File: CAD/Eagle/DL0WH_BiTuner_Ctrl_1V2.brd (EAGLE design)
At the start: 96.5 x 73 mm, 141 parts, among them Q0321 ABS07-32.768KHZ, U0101 STM32L476RXT_64PIN_LDO, U0601 MC33996, U0701 MC33996, U0801 MC33996, U0921 TS5A23166, U0951 OPA354, U1001 MAX232_SOIC16, U1101 MAX232_SOIC16, U1201 LM53603-Q1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

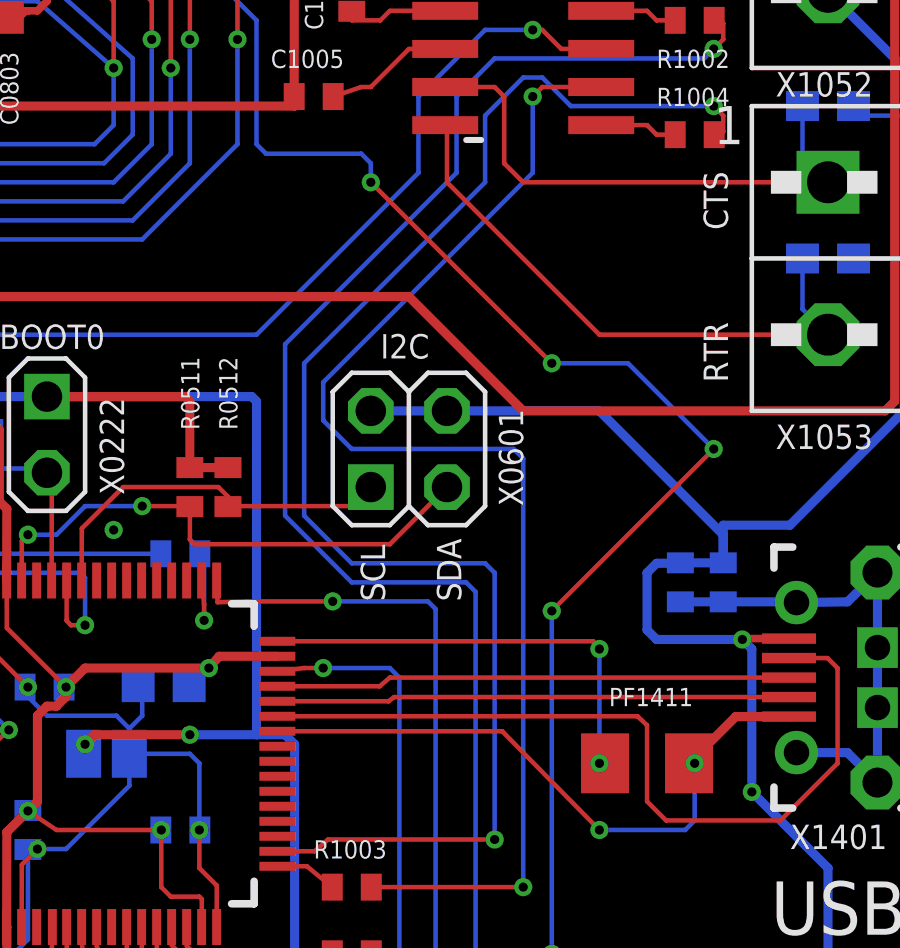
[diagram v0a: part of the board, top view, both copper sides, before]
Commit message: HW_1V2 - CAD/Eagle - add CRS08 to power the 5V rail when no 12V is attached
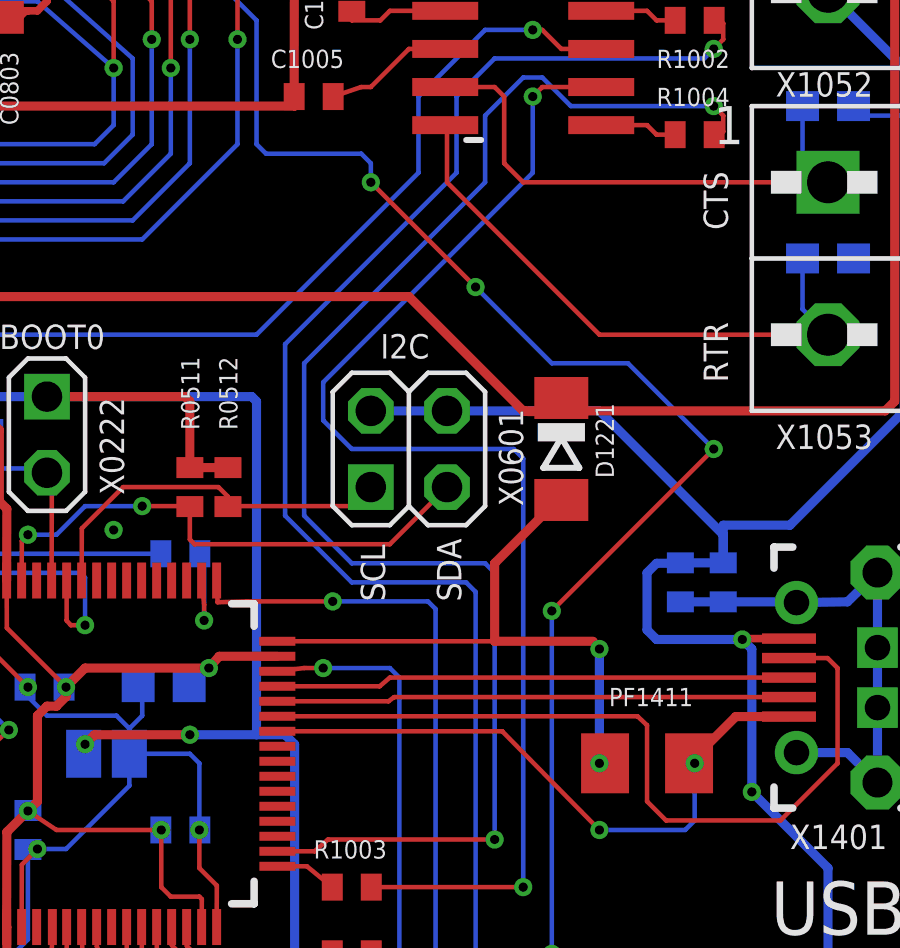
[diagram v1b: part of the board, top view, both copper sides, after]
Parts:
- added D1221: CRS08, df4iah_diode:SOD80C
- C0311: value 18pF -> 22pF
- C0332: value 8.2pF -> 18pF
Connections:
- net +5V: now also D1221.C
- net VDDUSB: now also D1221.A
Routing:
- net VDDUSB: track 15.1 -> 20.8 mm
- net +5V: track 286.2 -> 287.6 mm
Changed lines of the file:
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@@
 <attribute name="VALUE" x="61.08" y="24.5575" size="0.6096" layer="27" font="vector" ratio="10" rot="R180"/>
 </element>
-<element name="C0311" library="df4iah_rcl" package="C0402" value="18pF" x="57.62625" y="18.7325" smashed="yes" rot="R270">
+<element name="C0311" library="df4iah_rcl" package="C0402" value="22pF" x="57.62625" y="18.7325" smashed="yes" rot="R270">
 <attribute name="NAME" x="56.515" y="17.30375" size="0.6096" layer="25" font="vector" ratio="10" rot="R90"/>
 <attribute name="VALUE" x="55.72125" y="19.3675" size="0.6096" layer="27" font="vector" ratio="10" rot="R270"/>
@@
 <attribute name="VALUE" x="74.93" y="7.14375" size="0.6096" layer="28" font="vector" ratio="10" rot="MR180"/>
 </element>
-<element name="C0332" library="df4iah_rcl" package="C0402" value="8.2pF" x="60.96" y="24.4475" smashed="yes" rot="R90">
+<element name="C0332" library="df4iah_rcl" package="C0402" value="18pF" x="60.96" y="24.4475" smashed="yes" rot="R90">
 <attribute name="NAME" x="60.16625" y="23.1775" size="0.6096" layer="25" font="vector" ratio="10" rot="R90"/>
 <attribute name="VALUE" x="62.865" y="23.8125" size="0.6096" layer="27" font="vector" ratio="10" rot="R90"/>
@@
 <attribute name="VALUE" x="76.2" y="1.27" size="0.8128" layer="27" font="vector" ratio="15"/>
 </element>
+<element name="D1221" library="df4iah_diode" package="SOD80C" value="CRS08" x="83.82" y="29.21" rot="R270"/>
 </elements>
 <signals>
@@
 <via x="10.16" y="33.02" extent="1-16" drill="0.3048"/>
 <via x="17.62125" y="26.51125" extent="1-16" drill="0.3048"/>
+<wire x1="65.745" y1="56.72" x2="68.58" y2="58.42" width="0" layer="19" extent="1-1"/>
+<wire x1="15.3875" y1="53.295" x2="14.2875" y2="53.295" width="0" layer="19" extent="1-1"/>
+<wire x1="13.1875" y1="53.295" x2="14.2875" y2="53.295" width="0" layer="19" extent="1-1"/>
+<wire x1="15.3875" y1="54.595" x2="15.3875" y2="53.295" width="0" layer="19" extent="1-1"/>
+<wire x1="14.2875" y1="54.595" x2="15.3875" y2="54.595" width="0" layer="19" extent="1-1"/>
+<wire x1="14.2875" y1="55.245" x2="14.2875" y2="54.595" width="0" layer="19" extent="1-1"/>
+<wire x1="14.2875" y1="55.245" x2="14.2875" y2="55.245" width="0" layer="19" extent="1-16"/>
+<wire x1="14.2875" y1="55.895" x2="14.2875" y2="55.245" width="0" layer="19" extent="1-1"/>
+<wire x1="15.3875" y1="55.895" x2="14.2875" y2="55.895" width="0" layer="19" extent="1-1"/>
+<wire x1="13.1875" y1="55.895" x2="14.2875" y2="55.895" width="0" layer="19" extent="1-1"/>
+<wire x1="13.1875" y1="54.595" x2="14.2875" y2="54.595" width="0" layer="19" extent="1-1"/>
+<wire x1="15.3875" y1="57.195" x2="15.3875" y2="55.895" width="0" layer="19" extent="1-1"/>
+<wire x1="14.2875" y1="57.195" x2="15.3875" y2="57.195" width="0" layer="19" extent="1-1"/>
+<wire x1="13.1875" y1="57.195" x2="14.2875" y2="57.195" width="0" layer="19" extent="1-1"/>
+<wire x1="55.88" y1="20.32" x2="57.62625" y2="18.0825" width="0" layer="19" extent="1-1"/>
+<wire x1="17.62125" y1="26.51125" x2="14.605" y2="28.2575" width="0" layer="19" extent="1-1"/>
+<wire x1="68.8975" y1="26.51125" x2="65.3375" y2="27.21375" width="0" layer="19" extent="1-1"/>
+<wire x1="10.16" y1="33.02" x2="13.97" y2="31.75" width="0" layer="19" extent="16-16"/>
 </signal>
 <signal name="VDDUSB">
 <contactref element="PF1411" pad="2"/>
 <contactref element="U0101" pad="48"/>
-<wire x1="74.355" y1="22.8" x2="84.8825" y2="22.8" width="0.1524" layer="1"/>
+<wire x1="74.355" y1="22.8" x2="81.5975" y2="22.8" width="0.1524" layer="1"/>
+<wire x1="81.5975" y1="22.8" x2="84.8825" y2="22.8" width="0.3048" layer="1"/>
 <wire x1="84.8825" y1="22.8" x2="85.09" y2="22.5425" width="0.1524" layer="1"/>
 <via x="85.09" y="22.5425" extent="1-16" drill="0.3048"/>
-<wire x1="85.09" y1="22.5425" x2="85.09" y2="18.7325" width="0.1524" layer="16"/>
+<wire x1="85.09" y1="22.5425" x2="85.09" y2="18.7325" width="0.3048" layer="16"/>
 <via x="85.09" y="18.7325" extent="1-16" drill="0.3048"/>
 <wire x1="85.09" y1="18.7325" x2="85.09" y2="18.92" width="0.1524" layer="1"/>
 <wire x1="85.09" y1="18.92" x2="85.2775" y2="18.7325" width="0.1524" layer="1"/>
+<contactref element="D1221" pad="A"/>
+<wire x1="83.82" y1="27.51" x2="83.7075" y2="27.51" width="0.3048" layer="1"/>
+<wire x1="83.7075" y1="27.51" x2="81.5975" y2="25.4" width="0.3048" layer="1"/>
+<wire x1="81.5975" y1="25.4" x2="81.5975" y2="22.8" width="0.3048" layer="1"/>
 </signal>
 <signal name="MCU_VREF_M">
@@
 <wire x1="86.0575" y1="51.1175" x2="86.375" y2="51.435" width="0.3048" layer="1"/>
 <wire x1="11.7475" y1="47.625" x2="12.0375" y2="47.625" width="0.1524" layer="1"/>
+<contactref element="D1221" pad="C"/>
+<wire x1="82.55" y1="30.48" x2="83.82" y2="30.91" width="0.3048" layer="1" curve="60"/>
 </signal>
 <signal name="MP_CAT_RXD_R">
@@
 <wire x1="77.47" y1="38.735" x2="77.47" y2="38.1" width="0.1524" layer="16"/>
 <via x="77.47" y="38.1" extent="1-16" drill="0.3048"/>
-<wire x1="77.47" y1="38.1" x2="83.5025" y2="32.0675" width="0.1524" layer="1"/>
-<via x="83.5025" y="32.0675" extent="1-16" drill="0.3048"/>
+<wire x1="77.47" y1="38.1" x2="80.9625" y2="34.6075" width="0.1524" layer="1"/>
+<via x="80.9625" y="34.6075" extent="1-16" drill="0.3048"/>
+<wire x1="80.9625" y1="34.6075" x2="83.5025" y2="32.0675" width="0.1524" layer="16"/>
 <wire x1="83.5025" y1="32.0675" x2="86.0425" y2="32.0675" width="0.1524" layer="16"/>
 <wire x1="86.0425" y1="32.0675" x2="88.9" y2="29.21" width="0.1524" layer="16"/>

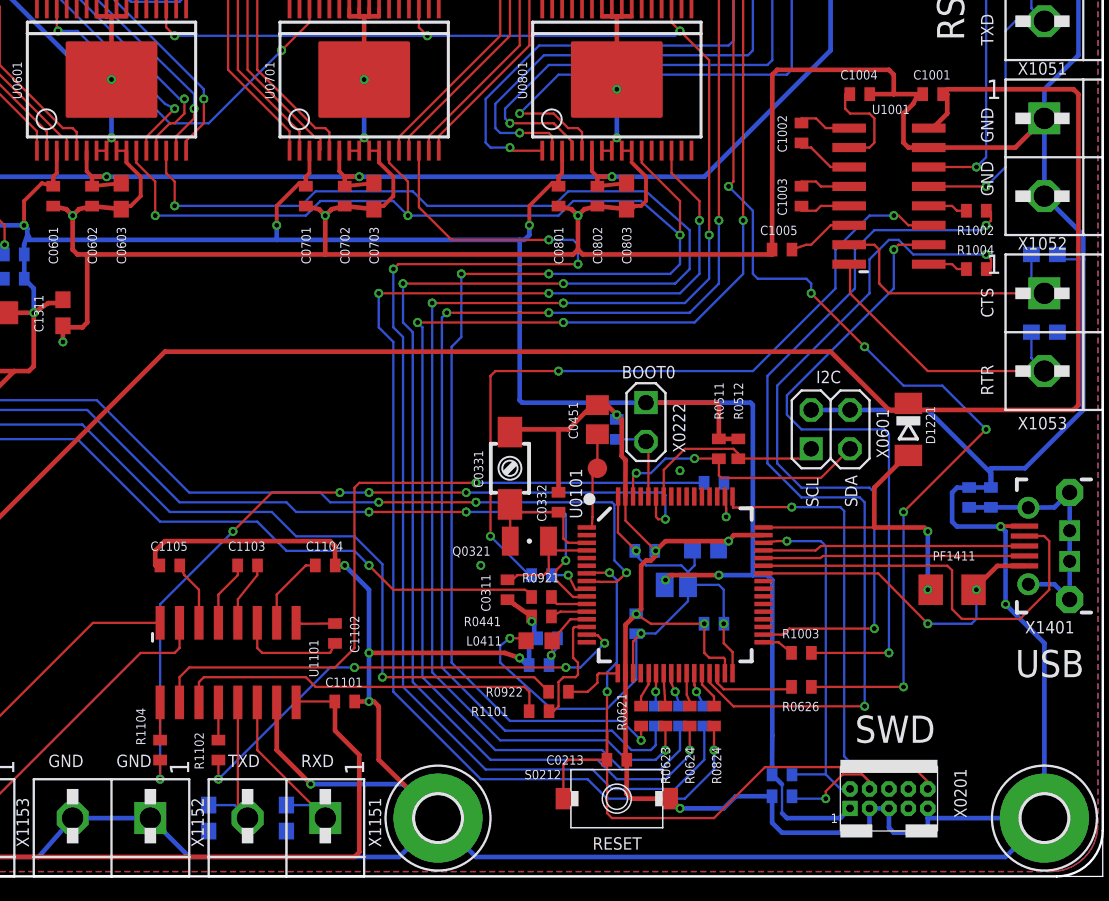
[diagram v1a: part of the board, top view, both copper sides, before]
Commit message: HW_1V2 - CAD/Eagle - edge connectors need more distance
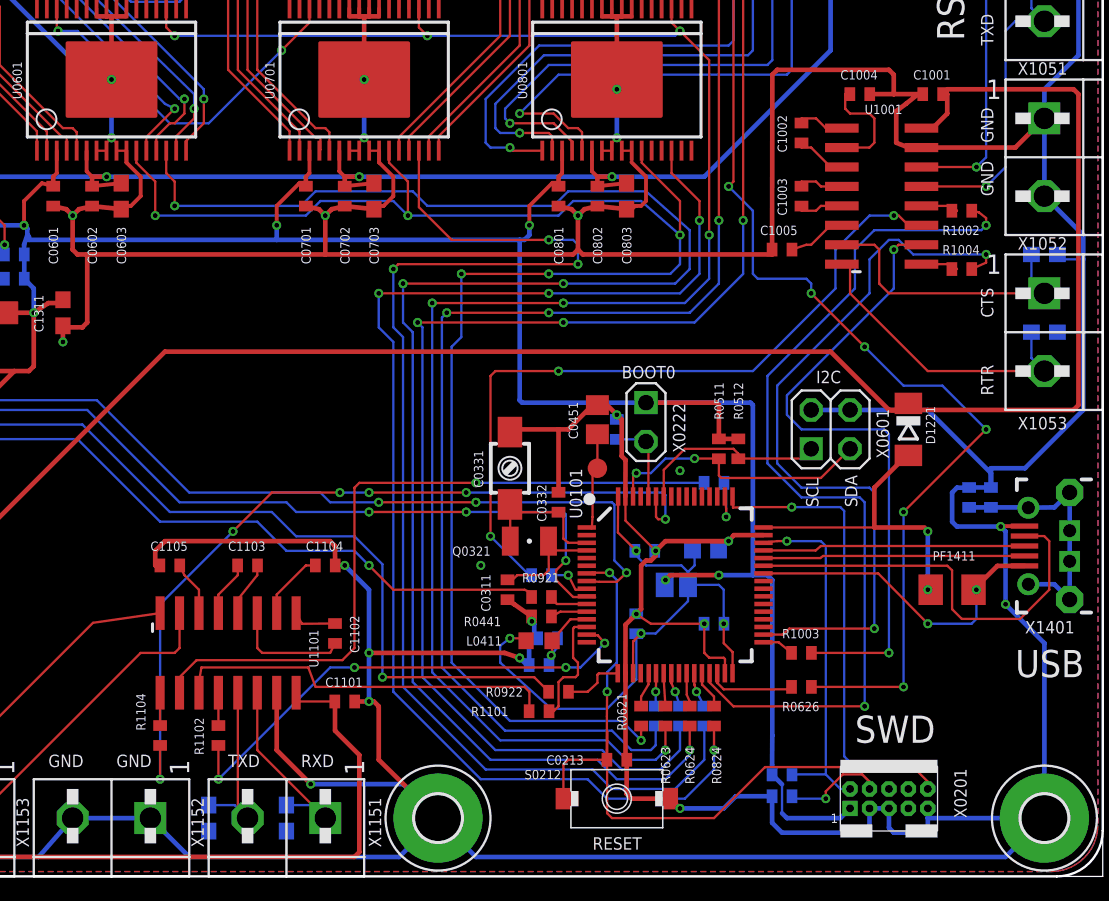
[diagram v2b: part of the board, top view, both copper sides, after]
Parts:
- moved R1002 0.95 mm to (87.3, 43.5)
- moved R1004 0.95 mm to (87.3, 39.7)
- moved R1102 0.95 mm to (38.7, 9.21)
- moved R1104 0.95 mm to (34.9, 9.21)
- moved U1101 0.63 mm to (39.4, 14.6)
- moved U1001 0.48 mm to (82.1, 44.5)
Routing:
- net GND: track 855.7 -> 857.1 mm
- net +5V: track 287.6 -> 288.5 mm
- net PA1: track 31.6 -> 32.5 mm
- net PB7: track 52.4 -> 53.4 mm
- net MP_CAT_RXD_R: track 24.7 -> 25.4 mm
- net MP_CAT_CTS_R: track 47.3 -> 46.7 mm
- net CAT_DTE_TXD: track 10.7 -> 11.4 mm
- net CAT_DTE_RXD: track 12.3 -> 12.9 mm
- net CAT_MX_VP: track 5.16 -> 4.52 mm
- net CAT_MX_C2P: track 4.19 -> 3.56 mm
- net CAT_MX_C2M: track 4.28 -> 3.64 mm
- net CAT_MX_C1N: track 7.24 -> 7.87 mm
- net CAT_DTE_CTS: track 22.5 -> 23.1 mm
- net CAT_MX_VM: track 4.21 -> 3.58 mm

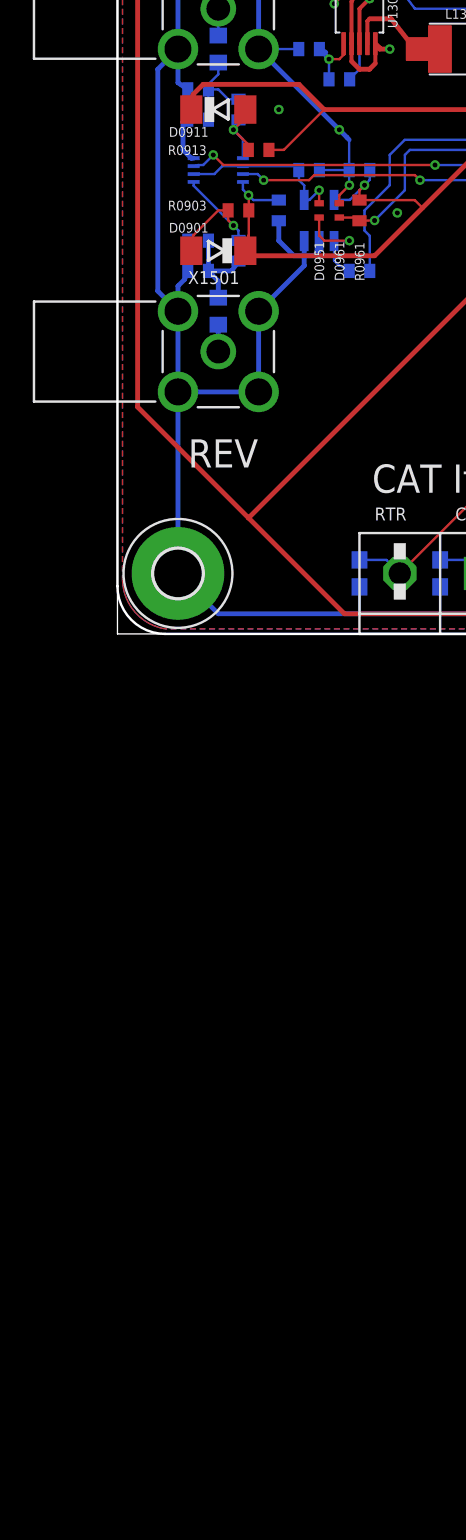
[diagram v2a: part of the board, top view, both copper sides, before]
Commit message: HW_1V2 - CAD/Eagle - LogAmp added
Signed-off-by: Ulrich Habel <espero7757@gmx.net>
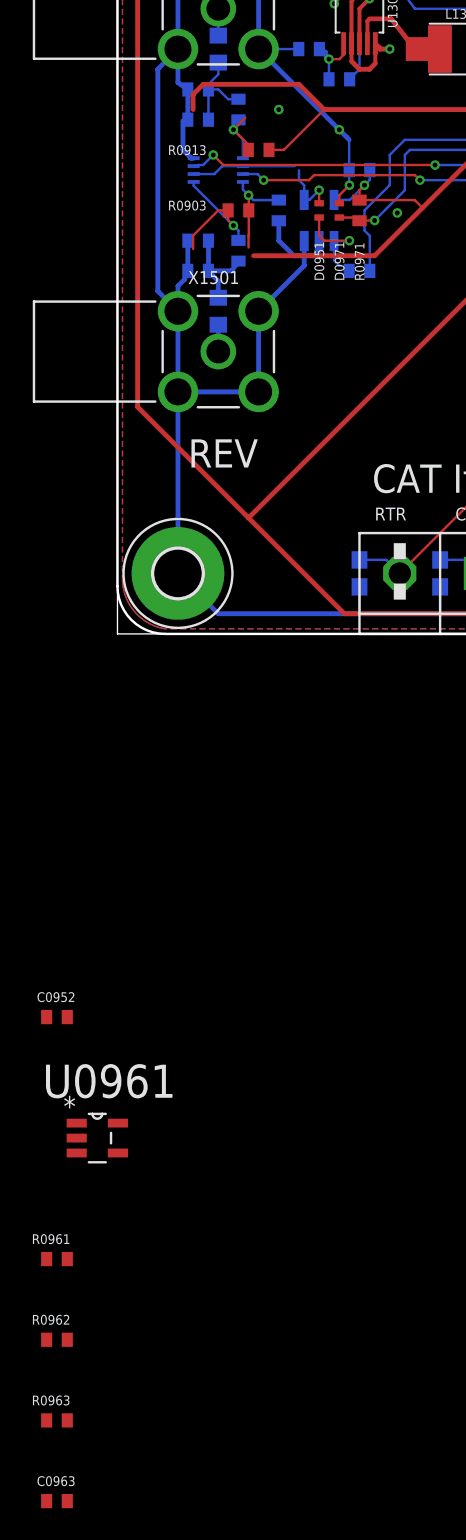
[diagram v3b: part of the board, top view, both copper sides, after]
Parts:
- removed D0901, D0911: CRS08, df4iah_diode:SOD80C
- removed R0951: 1MR, df4iah_rcl:R0402
- added C0952: 100nF, df4iah_rcl:C0402
- added C0963: 100pF, df4iah_rcl:C0402
- added R0962: 4.7kR, df4iah_rcl:R0402
- added R0963: 18kR, df4iah_rcl:R0402
- added R0971: 10kR, df4iah_rcl:R0402
- added U0961: OPA354, df4iah_opamp:SOT-23-5
- C0901, C0911: value 10nF -> 1nF
- R0903, R0913: value 100kR -> 150kR
- R0961: value 10kR -> 1kR
- moved R0961 68.7 mm to (-3.81, -39.4), turned to 0 degrees
- renumbered D0961 to D0971, R0952 to R0972
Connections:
- removed net SWR_OP_OUT: D0951.C, R0972.1, U0951.1
- new net -1V5: C0952.1, U0951.2, U0961.2
- new net SWR_OP1_OUT: D0951.C, R0961.1, U0951.1
- new net SWR_OP2_IN: C0963.1, R0961.2, R0962.1, R0963.1, U0961.4
- new net SWR_OP2_OUT: C0963.2, R0963.2, R0972.1, U0961.1
- net +3V3: now also R0962.2, R0971.1, U0961.5; no longer D0901.C, D0911.C, R0961.1
- net GND: now also C0952.2, U0961.3; no longer R0951.1, U0951.2
- net PC2: now also R0971.2; no longer R0961.2
- net SWR_IN_FWD: no longer D0901.A
- net SWR_IN_REV: no longer D0911.A
- net SWR_SEL_PWR: no longer R0951.2
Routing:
- net SWR_OP_OUT: track 6.56 -> 0.00 mm, vias 1 -> 0
- net SWR_OP1_OUT: track 0.00 -> 5.95 mm, vias 0 -> 1
- net GND: track 857.1 -> 854.6 mm
- net +3V3: track 221.3 -> 220.2 mm
- net SWR_IN_REV: track 6.03 -> 5.50 mm
